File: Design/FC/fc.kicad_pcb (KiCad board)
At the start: 4 copper layers, 70.8 x 100 mm, 115 parts, among them J1 AMASS_XT60PW-M, U1 STM32H747BIT6, U2 INA219AIDCNT

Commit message: finished filling out bom
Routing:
- net GND: vias 125 -> 132
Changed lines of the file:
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@@
 		(tags "Through hole pin header THT 2x01 2.54mm double row")
 		(property "Reference" "RM1"
-			(at 4.725 0.15 0)
+			(at 4.848595 0.092187 0)
 			(layer "F.SilkS")
 			(effects
@@
 		(tags "capacitor handsolder")
 		(property "Reference" "C18"
-			(at 2.233634 -0.349998 90)
+			(at 2.938323 -0.0457 180)
 			(layer "F.SilkS")
 			(effects
@@
 		(tags "Integrated Circuit")
 		(property "Reference" "FLASH1"
-			(at -3.871134 -3.905 0)
+			(at -1.123883 -3.95832 0)
 			(layer "F.SilkS")
 			(effects
@@
 		(tags "capacitor handsolder")
 		(property "Reference" "C49"
-			(at 3.091366 -0.14 180)
+			(at 2.880427 -0.001132 180)
 			(layer "F.SilkS")
 			(effects
@@
 		(tags "BMP390 ")
 		(property "Reference" "BARO1"
-			(at 3.250001 1 90)
+			(at 3.111728 0.88724 90)
 			(unlocked yes)
 			(layer "F.SilkS")
@@
 		(tags "resistor handsolder")
 		(property "Reference" "R14"
-			(at 2.9125 0.75 0)
+			(at 0.175781 1.367581 0)
 			(layer "F.SilkS")
 			(effects
@@
 		(at 205.25 80.06 90)
 		(property "Reference" "R2"
-			(at -0.94 1.75 0)
+			(at 2.252981 -0.095315 0)
 			(layer "F.SilkS")
 			(effects
@@
 			(at 0 4.792863 0)
 			(layer "F.SilkS")
+			(hide yes)
 			(effects
 				(font
@@
 		(at 201.75 81.42 -90)
 		(property "Reference" "C2"
-			(at 1.33 -2.5 90)
+			(at -2.892277 -0.025384 180)
 			(layer "F.SilkS")
 			(effects
@@
 		(tags "MMC5983MA ")
 		(property "Reference" "MAG1"
-			(at -0.225001 -4.7054 0)
+			(at 0 2.580542 90)
 			(unlocked yes)
 			(layer "F.SilkS")
@@
 		(tags "capacitor handsolder")
 		(property "Reference" "C47"
-			(at 2.0625 0 0)
+			(at 2.348303 -0.035836 0)
 			(layer "F.SilkS")
 			(effects
@@
 		(at 229.19914 97.212861 90)
 		(property "Reference" "RF1"
-			(at 1.212861 -4.69914 90)
+			(at 7.038275 2.629577 180)
 			(layer "F.SilkS")
 			(effects
@@
 		(tags "capacitor handsolder")
 		(property "Reference" "C1"
-			(at 0 -1.5 0)
+			(at 0.761332 -1.343358 0)
 			(layer "F.SilkS")
 			(effects
@@
 			(at 0.055736 4.588911 0)
 			(layer "F.SilkS")
+			(hide yes)
 			(effects
 				(font
@@
 			(at 4.447056 -0.052944 0)
 			(layer "F.SilkS")
+			(hide yes)
 			(effects
 				(font
@@
 		(tags "LED")
 		(property "Reference" "LED8"
-			(at -2.851384 -2.990511 0)
+			(at 3.393409 -0.111342 0)
 			(layer "F.SilkS")
 			(effects
@@
 		(tags "capacitor handsolder")
 		(property "Reference" "C46"
-			(at -1.999901 0.05 90)
+			(at -1.349283 1.236329 180)
 			(layer "F.SilkS")
 			(effects
@@
 		(tags "resistor handsolder")
 		(property "Reference" "R3"
-			(at -0.869683 -1.255376 0)
+			(at -0.026721 -1.236626 0)
 			(layer "F.SilkS")
 			(effects
@@
 			(at 0 -4.15 0)
 			(layer "F.SilkS")
+			(hide yes)
 			(effects
 				(font
@@
 		(tags "capacitor handsolder")
 		(property "Reference" "C10"
-			(at -3.299098 -0.265163 0)
+			(at -3.351703 0.175202 0)
 			(layer "F.SilkS")
 			(effects
@@
 		(tags "capacitor handsolder")
 		(property "Reference" "C44"
-			(at -0.1375 1.2 0)
+			(at -0.095737 1.378329 0)
 			(layer "F.SilkS")
 			(effects
@@
 	)
 	(gr_text "GPS"
-		(at 217.25 143.75 0)
+		(at 222.471509 147.558988 0)
 		(layer "F.SilkS")
 		(effects
@@
 	)
 	(gr_text "+"
-		(at 213 93.75 0)
+		(at 210.405861 90.592182 0)
 		(layer "F.SilkS")
 		(effects
@@
 	)
 	(gr_text "+"
-		(at 205.5 88 0)
+		(at 205.523045 90.811723 0)
 		(layer "F.SilkS")
 		(effects
@@
 	)
 	(via
-		(at 213.65 91.7)
+		(at 213.65 91.6)
 		(size 1)
 		(drill 0.6)
@@
 	)
 	(via
-		(at 214.85 91.7)
+		(at 214.85 91.6)
 		(size 1)
 		(drill 0.6)
@@
 	)
 	(via
-		(at 216.1 91.7)
+		(at 216.1 91.6)
 		(size 1)
 		(drill 0.6)
@@
 	)
 	(via
-		(at 218.6 91.7)
+		(at 218.6 91.6)
 		(size 1)
 		(drill 0.6)
@@
 	)
 	(via
-		(at 212.4 91.7)
+		(at 212.4 91.6)
 		(size 1)
 		(drill 0.6)
@@
 	)
 	(via
-		(at 206.25 91.7)
+		(at 206.25 91.6)
 		(size 1)
 		(drill 0.6)
@@
 	)
 	(via
-		(at 219.85 91.7)
+		(at 219.85 91.6)
 		(size 1)
 		(drill 0.6)
@@
 	)
 	(via
-		(at 207.45 91.7)
+		(at 207.45 91.6)
 		(size 1)
 		(drill 0.6)
@@
 	)
 	(via
-		(at 208.65 91.7)
+		(at 208.65 91.6)
 		(size 1)
 		(drill 0.6)
@@
 	)
 	(via
-		(at 209.9 91.7)
+		(at 209.9 91.6)
 		(size 1)
 		(drill 0.6)
@@
 	)
 	(via
-		(at 217.35 91.7)
+		(at 217.35 91.6)
 		(size 1)
 		(drill 0.6)
@@
 	)
 	(via
-		(at 211.15 91.7)
+		(at 211.15 91.6)
 		(size 1)
 		(drill 0.6)
@@
 	)
 	(via
-		(at 204.101114 122.777862)
+		(at 204.078954 122.777862)
 		(size 0.8)
 		(drill 0.4)
@@
 	)
 	(via
-		(at 186.25 79.5)
+		(at 186 79.5)
 		(size 0.8)
 		(drill 0.4)
@@
 	)
 	(via
+		(at 218.991014 95.905465)
+		(size 0.8)
+		(drill 0.4)
+		(layers "F.Cu" "B.Cu")
+		(net 160)
+	)
+	(via
 		(at 231.5 67.25)
 		(size 0.8)
@@
 	)
 	(via
-		(at 204.123274 131.220938)
+		(at 204.078954 131.220938)
 		(size 0.8)
 		(drill 0.4)
@@
 	)
 	(via
-		(at 189.5 85.25)
+		(at 189.25 85.25)
+		(size 0.8)
+		(drill 0.4)
+		(layers "F.Cu" "B.Cu")
+		(net 160)
+	)
+	(via
+		(at 218.991014 94.5)
 		(size 0.8)
 		(drill 0.4)
@@
 	)
 	(via
+		(at 218.991014 97.270038)
+		(size 0.8)
+		(drill 0.4)
+		(layers "F.Cu" "B.Cu")
+		(net 160)
+	)
+	(via
+		(at 221.84238 124.82285)
+		(size 0.8)
+		(drill 0.4)
+		(layers "F.Cu" "B.Cu")
+		(net 160)
+	)
+	(via
 		(at 194.3 96.65)
 		(size 0.8)
@@
 	)
 	(via
-		(at 186.25 77.5)
+		(at 186 77.5)
 		(size 0.8)
 		(drill 0.4)
@@
 	)
 	(via
-		(at 186.25 83.25)
+		(at 186 83.25)
+		(size 0.8)
+		(drill 0.4)
+		(layers "F.Cu" "B.Cu")
+		(net 160)
+	)
+	(via
+		(at 177.9798 139.322942)
 		(size 0.8)
 		(drill 0.4)
@@
 	)
 	(via
+		(at 175.209762 139.300782)
+		(size 0.8)
+		(drill 0.4)
+		(layers "F.Cu" "B.Cu")
+		(net 160)
+	)
+	(via
 		(at 192.75 135.5)
 		(size 0.8)
@@
 	)
 	(via
-		(at 200.20568 126.847)
+		(at 200.25 126.847)
 		(size 0.8)
 		(drill 0.4)
@@
 	)
 	(via
-		(at 189.5 77.5)
+		(at 189.25 77.5)
 		(size 0.8)
 		(drill 0.4)
@@
 	)
 	(via
-		(at 189.5 79.5)
+		(at 189.25 79.5)
 		(size 0.8)
 		(drill 0.4)
@@
 	)
 	(via
+		(at 221.82022 127.592888)
+		(size 0.8)
+		(drill 0.4)
+		(layers "F.Cu" "B.Cu")
+		(net 160)
+	)
+	(via
 		(at 208.92219 73.119171)
 		(size 0.6)
@@
 	)
 	(via
-		(at 198.65 67.5)
+		(at 198.763368 67.443055)
 		(size 0.8)
 		(drill 0.4)
@@
 	)
 	(via
-		(at 189.5 83.25)
+		(at 189.25 83.25)
 		(size 0.8)
 		(drill 0.4)
@@
 	)
 	(via
-		(at 186.25 85.25)
+		(at 186 85.25)
 		(size 0.8)
 		(drill 0.4)

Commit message: layout
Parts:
- C2, C3: footprint Lib:CAP_GMK325BJ226MM-T-CAPC3225X280N -> Capacitor_SMD:C_1210_3225Metric_Pad1.33x2.70mm_HandSolder
- C4, C51: footprint Lib:CAP_C225K4REC7210_0805 -> Capacitor_SMD:C_0805_2012Metric_Pad1.18x1.45mm_HandSolder
- C46: footprint Capacitor_SMD:C_0603_1608Metric_Pad1.08x0.95mm_HandSolder -> Capacitor_SMD:C_0805_2012Metric_Pad1.18x1.45mm_HandSolder
- C5, C6: footprint Lib:CAP_C0805X104K5RAC3316_0805_100nF -> Capacitor_SMD:C_0805_2012Metric_Pad1.18x1.45mm_HandSolder
- FLASH1: value SON127P800X600X80-9N-D -> W25N01GWZEIG
- J1: value AMASS_XT60PW-M -> XT60PW-M
- moved C45 0.18 mm to (173.5, 119.7)
- moved C46 0.16 mm to (176.2, 118.8)
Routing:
- net GND: track 207.9 -> 213.9 mm, vias 132 -> 135
- net +3.3V: track 256.5 -> 258.7 mm, vias 45 -> 46
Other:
- board text removed: "RX"

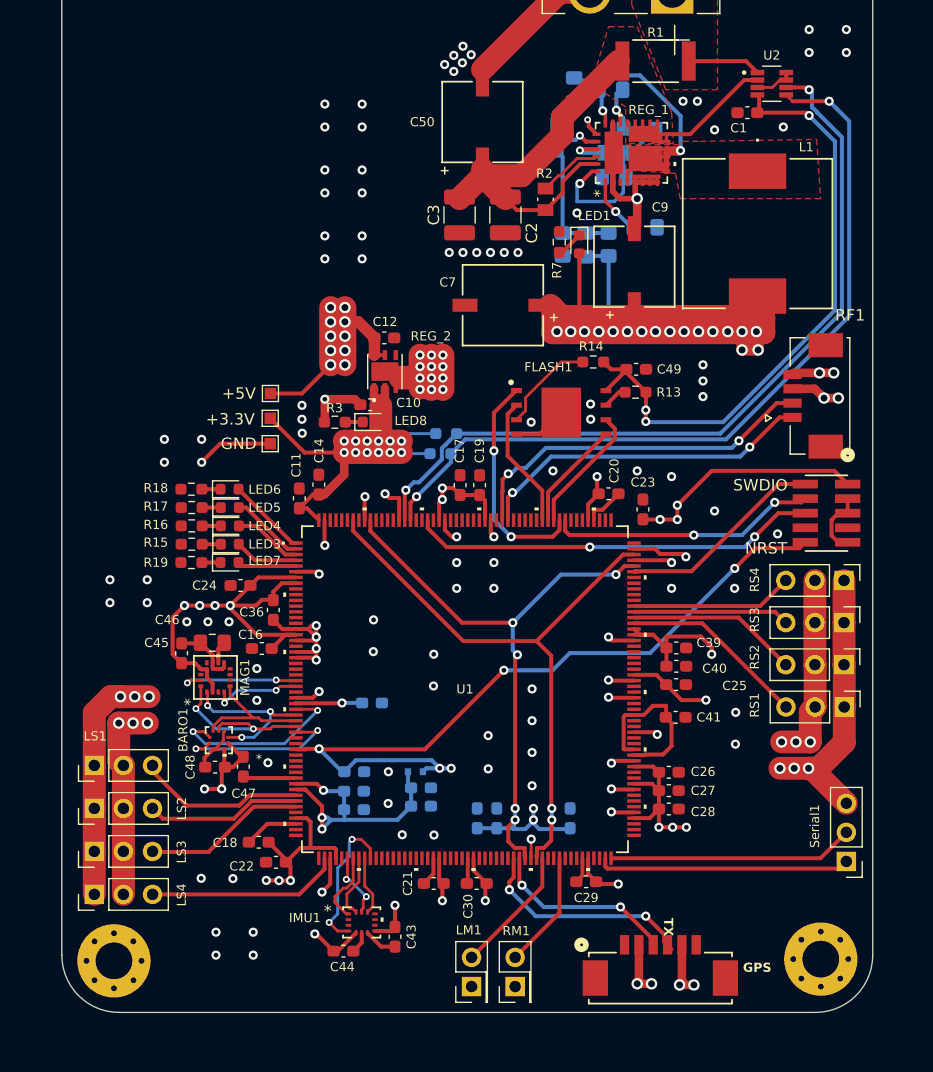
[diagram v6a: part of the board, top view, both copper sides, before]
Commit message: edited servo connector layout to support larger connectors
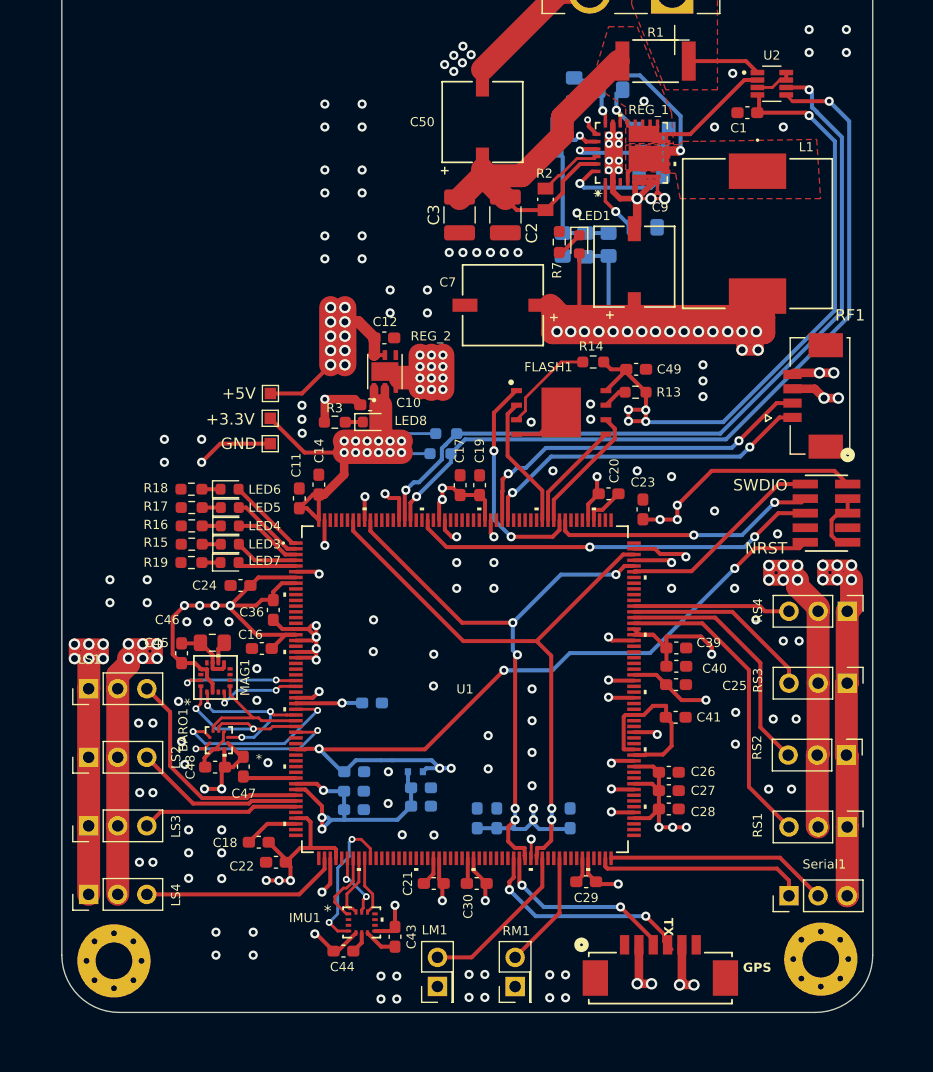
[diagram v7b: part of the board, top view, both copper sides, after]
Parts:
- moved RS1 10.5 mm to (231.6, 134.8)
- moved RS2 7.89 mm to (231.5, 128.5)
- moved LS1 6.71 mm to (165.4, 122.8)
- moved Serial1 5.83 mm to (226.5, 140.8), turned to 90 degrees
- moved RS3 5.29 mm to (231.6, 122.3)
- moved LS2 4.49 mm to (165.4, 128.7)
- moved R20 3.31 mm to (214.6, 76.0)
- moved C51 3.22 mm to (214.5, 78.0)
- moved LM1 2.98 mm to (195.8, 148.7)
- moved RS4 2.70 mm to (231.6, 116.0)
- moved LS3 2.29 mm to (165.4, 134.7)
- moved D1 1.15 mm to (214.6, 73.9)
- moved LS4 0.50 mm to (165.4, 140.7)
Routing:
- net +5V: track 139.3 -> 165.7 mm, vias 37 -> 43
- net GND: track 213.9 -> 240.0 mm, vias 135 -> 187
- net R_SERVO_1_SIGNAL: track 16.3 -> 26.9 mm
- net R_SERVO_2_SIGNAL: track 14.9 -> 21.7 mm
- net +3.3V: track 258.7 -> 265.0 mm, vias 46 -> 48
- net L_SERVO_1_SIGNAL: track 14.6 -> 19.8 mm
- net DEBUG_TX: track 22.1 -> 18.6 mm
- net REG_1_PG: track 3.64 -> 6.95 mm
- net R_SERVO_3_SIGNAL: track 13.6 -> 16.9 mm
- net L_MOTOR_1_SIGNAL: track 11.2 -> 14.2 mm
- net DEBUG_RX: track 21.5 -> 19.5 mm
- net L_SERVO_2_SIGNAL: track 13.5 -> 14.8 mm
- net /Power/REG_1_VDD: track 15.0 -> 14.0 mm
- net REG_1_BST: track 5.09 -> 5.65 mm

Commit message: extended smd pads for lga packages
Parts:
- moved C46 0.88 mm to (176.2, 117.9)
- moved C43 0.88 mm to (193.0, 144.4)
- moved C44 0.85 mm to (187.6, 146.5)
- moved C45 0.55 mm to (173.3, 119.2)
- moved C48 0.40 mm to (176.4, 130.0)
- moved C47 0.36 mm to (179.2, 129.6)
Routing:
- net GND: track 240.0 -> 243.1 mm, vias 187 -> 195
- net BARO_SPI_MOSI: track 15.4 -> 17.2 mm
- net EXT_3_DEV_INT: track 10.9 -> 12.2 mm
- net +3.3V: track 265.0 -> 266.0 mm
- net Net-(MAG1-CAP): track 1.96 -> 2.87 mm
- net EXT_5_DEV_IMU: track 12.9 -> 13.6 mm
- net BARO_SPI_SCK: track 14.4 -> 15.1 mm
